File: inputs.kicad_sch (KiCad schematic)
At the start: 2 parts, among them J4 BUTTON, J6 ROTARY_ENCODER

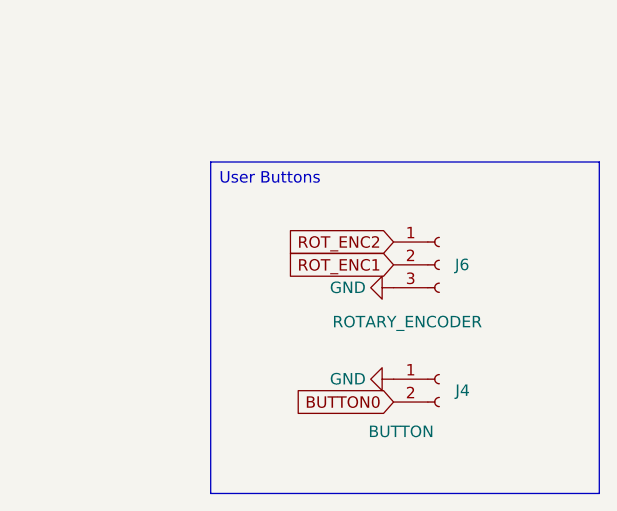
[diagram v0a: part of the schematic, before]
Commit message: Routed RF Core
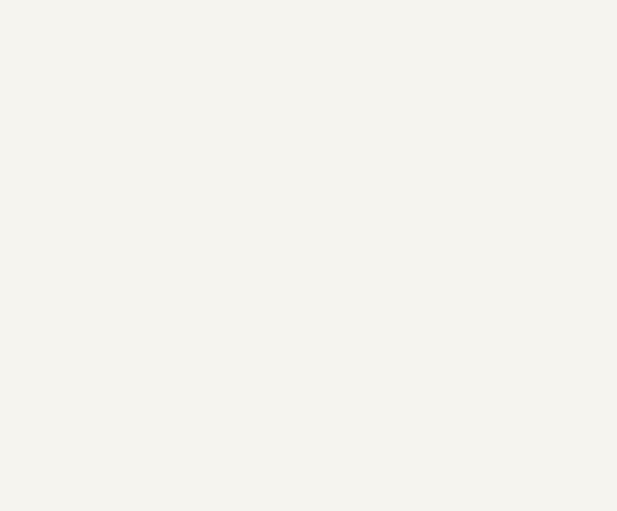
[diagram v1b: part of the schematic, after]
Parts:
- removed J4: BUTTON, Connector_PinHeader_1.27mm:PinHeader_1x02_P1.27mm_Vertical, symbol Connector:Conn_01x02_Socket
- removed J6: ROTARY_ENCODER, Connector_PinHeader_1.27mm:PinHeader_1x03_P1.27mm_Vertical, symbol Connector:Conn_01x03_Socket
